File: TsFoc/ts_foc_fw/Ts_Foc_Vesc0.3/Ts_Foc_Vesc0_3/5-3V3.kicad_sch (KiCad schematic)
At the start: 6 parts, among them U2 AMS1117-3.3V

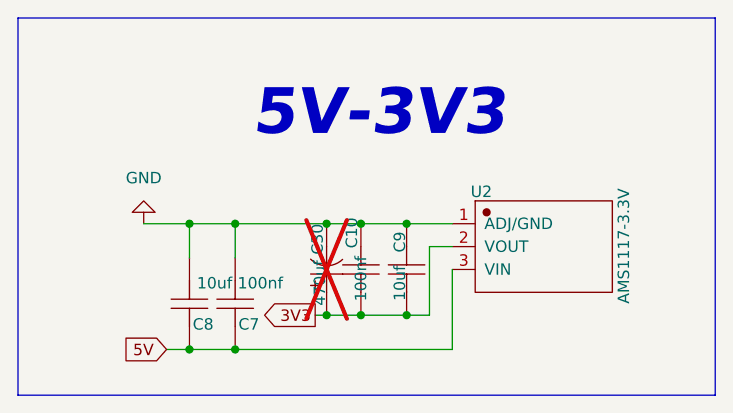
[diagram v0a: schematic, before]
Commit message: 添加tsfoc库 1. 实现简易电压位置闭环控制 2. 实现简易电压力矩闭环控制
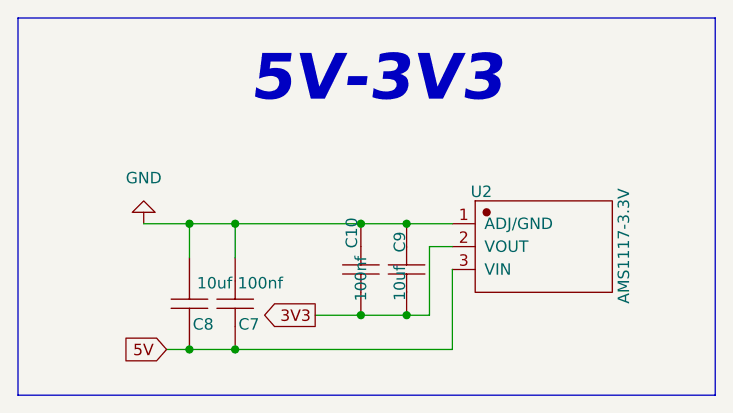
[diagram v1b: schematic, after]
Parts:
- removed C30: 470uf, Ts_Foc_Vo封装库:Cap_Electrolytic, symbol Ts_Foc_Vo符号库:Cap_Electrolytic
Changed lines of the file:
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@@
 	(text "5V-3V3\n"
 		(exclude_from_sim yes)
-		(at 247.142 23.368 0)
+		(at 246.888 19.558 0)
 		(effects
 			(font
@@
 	)
 	(junction
-		(at 241.3 35.56)
-		(diameter 0)
-		(color 0 0 0 0)
-	)
-	(junction
 		(at 226.06 35.56)
 		(diameter 0)
@@
 	)
 	(junction
-		(at 241.3 45.72)
-		(diameter 0)
-		(color 0 0 0 0)
-	)
-	(junction
 		(at 245.11 45.72)
 		(diameter 0)
@@
 	(wire
 		(pts
-			(xy 231.14 35.56) (xy 241.3 35.56)
+			(xy 231.14 35.56) (xy 245.11 35.56)
 		)
 		(stroke
@@
 	(wire
 		(pts
-			(xy 240.03 45.72) (xy 241.3 45.72)
+			(xy 240.03 45.72) (xy 245.11 45.72)
 		)
 		(stroke
@@
 	(wire
 		(pts
-			(xy 241.3 35.56) (xy 245.11 35.56)
-		)
-		(stroke
-			(width 0)
-			(type default)
-		)
-	)
-	(wire
-		(pts
 			(xy 223.52 49.53) (xy 226.06 49.53)
 		)
@@
 		(pts
 			(xy 250.19 45.72) (xy 252.73 45.72)
-		)
-		(stroke
-			(width 0)
-			(type default)
-		)
-	)
-	(wire
-		(pts
-			(xy 241.3 45.72) (xy 245.11 45.72)
 		)
 		(stroke
@@
 					(unit 1)
 				)
-			)
-		)
-	)
-	(symbol
-		(lib_id "Ts_Foc_Vo符号库:Cap_Electrolytic")
-		(at 241.3 40.64 90)
-		(unit 1)
-		(exclude_from_sim yes)
-		(in_bom no)
-		(on_board no)
-		(dnp yes)
-		(property "Reference" "C30"
-			(at 240.284 35.56 0)
-			(effects
-				(font
-					(size 1.27 1.27)
-				)
-				(justify right)
-			)
-		)
-		(property "Value" "470uf"
-			(at 240.538 39.624 0)
-			(effects
-				(font
-					(size 1.27 1.27)
-				)
-				(justify right)
-			)
-		)
-		(property "Footprint" "Ts_Foc_Vo封装库:Cap_Electrolytic"
-			(at 244.094 40.386 0)
-			(effects
-				(font
-					(size 1.27 1.27)
-				)
-				(hide yes)
-			)
-		)
-		(property "Datasheet" ""
-			(at 247.142 40.64 0)
-			(effects
-				(font
-					(size 1.27 1.27)
-				)
-				(hide yes)
-			)
-		)
-		(property "Description" ""
-			(at 241.3 40.64 0)
-			(effects
-				(font
-					(size 1.27 1.27)
-				)
-				(hide yes)
-			)
-		)
-		(property "SuppliersPartNumber" "C2960233"
-			(at 244.094 40.894 0)
-			(effects
-				(font
-					(size 1.27 1.27)
-				)
-				(hide yes)
-			)
-		)
-		(property "uuid" "std:f2c4c4acb06341a6b501ff67d9191846"
-			(at 244.094 40.894 0)
-			(effects
-				(font
-					(size 1.27 1.27)
-				)
-				(hide yes)
-			)
-		)
-		(pin "2"
-		)
-		(pin "1"
-		)
-		(instances
-			(project "Ts_Foc_Vo1_0"
-				(path "/0cbcabec-8024-48c7-ab91-86e279a5637e/97ee4039-d600-4608-b2ff-7d42036ea92c/e8a44f51-cbda-485e-b097-3ee1dbcae92f"
-					(reference "C30")
-					(unit 1)
-				)
